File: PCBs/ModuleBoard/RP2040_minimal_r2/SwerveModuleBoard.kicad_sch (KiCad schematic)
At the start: 52 parts, among them J1 USB_B_Micro, J2 Conn_01x02, J4 Conn_01x07, J5 Conn_01x06_Pin, J6 Conn_01x02, J7 Conn_01x06_Pin, J8 Conn_01x06, U1 NCP1117-3.3_SOT223, U2 W25Q128JVS, U3 RP2040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

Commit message: vault backup: 2025-04-24 00:27:01
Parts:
- removed J2: Conn_01x02, Connector_PinHeader_2.54mm:PinHeader_1x02_P2.54mm_Vertical, symbol Connector_Generic:Conn_01x02
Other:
- moved on the sheet: BTSEL1
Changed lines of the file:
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@@
 	(wire
 		(pts
+			(xy 20.32 125.73) (xy 17.78 125.73)
+		)
+		(stroke
+			(width 0)
+			(type default)
+		)
+	)
+	(wire
+		(pts
 			(xy 39.37 204.47) (xy 46.99 204.47)
 		)
@@
 	(wire
 		(pts
-			(xy 44.45 125.73) (xy 31.75 125.73)
-		)
-		(stroke
-			(width 0)
-			(type default)
-		)
-	)
-	(wire
-		(pts
 			(xy 214.63 76.2) (xy 223.52 76.2)
 		)
@@
 	(wire
 		(pts
-			(xy 31.75 128.27) (xy 33.02 128.27)
-		)
-		(stroke
-			(width 0)
-			(type default)
-		)
-	)
-	(wire
-		(pts
 			(xy 234.95 60.96) (xy 246.38 60.96)
 		)
@@
 	(wire
 		(pts
+			(xy 30.48 125.73) (xy 44.45 125.73)
+		)
+		(stroke
+			(width 0)
+			(type default)
+		)
+	)
+	(wire
+		(pts
 			(xy 229.87 142.24) (xy 245.11 142.24)
 		)
@@
 	(wire
 		(pts
-			(xy 33.02 128.27) (xy 33.02 129.54)
-		)
-		(stroke
-			(width 0)
-			(type default)
-		)
-	)
-	(wire
-		(pts
 			(xy 97.79 105.41) (xy 97.79 120.65)
 		)
@@
 		)
 	)
-	(label "~{USB_BOOT}"
-		(at 36.83 109.22 0)
-		(effects
-			(font
-				(size 1.27 1.27)
-			)
-			(justify left bottom)
-		)
-	)
 	(label "GPIO14"
 		(at 245.11 147.32 180)
@@
 	)
 	(symbol
-		(lib_id "Connector_Generic:Conn_01x02")
-		(at 26.67 125.73 0)
-		(mirror y)
-		(unit 1)
-		(exclude_from_sim no)
-		(in_bom yes)
-		(on_board yes)
-		(dnp no)
-		(property "Reference" "J2"
-			(at 25.4 121.92 0)
-			(effects
-				(font
-					(size 1.27 1.27)
-				)
-			)
-		)
-		(property "Value" "Conn_01x02"
-			(at 25.4 132.08 0)
-			(effects
-				(font
-					(size 1.27 1.27)
-				)
-			)
-		)
-		(property "Footprint" "Connector_PinHeader_2.54mm:PinHeader_1x02_P2.54mm_Vertical"
-			(at 26.67 125.73 0)
-			(effects
-				(font
-					(size 1.27 1.27)
-				)
-				(hide yes)
-			)
-		)
-		(property "Datasheet" "~"
-			(at 26.67 125.73 0)
-			(effects
-				(font
-					(size 1.27 1.27)
-				)
-				(hide yes)
-			)
-		)
-		(property "Description" ""
-			(at 26.67 125.73 0)
-			(effects
-				(font
-					(size 1.27 1.27)
-				)
-				(hide yes)
-			)
-		)
-		(pin "1"
-		)
-		(pin "2"
-		)
-		(instances
-			(project "RP2040_minimal_r2"
-				(path "/8c0b3d8b-46d3-4173-ab1e-a61765f77d61"
-					(reference "J2")
-					(unit 1)
-				)
-			)
-		)
-	)
-	(symbol
-		(lib_id "power:GND")
-		(at 33.02 129.54 0)
-		(unit 1)
-		(exclude_from_sim no)
-		(in_bom yes)
-		(on_board yes)
-		(dnp no)
-		(property "Reference" "#PWR02"
-			(at 33.02 135.89 0)
-			(effects
-				(font
-					(size 1.27 1.27)
-				)
-				(hide yes)
-			)
-		)
-		(property "Value" "GND"
-			(at 33.147 133.9342 0)
-			(effects
-				(font
-					(size 1.27 1.27)
-				)
-			)
-		)
-		(property "Footprint" ""
-			(at 33.02 129.54 0)
-			(effects
-				(font
-					(size 1.27 1.27)
-				)
-				(hide yes)
-			)
-		)
-		(property "Datasheet" ""
-			(at 33.02 129.54 0)
-			(effects
-				(font
-					(size 1.27 1.27)
-				)
-				(hide yes)
-			)
-		)
-		(property "Description" ""
-			(at 33.02 129.54 0)
-			(effects
-				(font
-					(size 1.27 1.27)
-				)
-				(hide yes)
-			)
-		)
-		(pin "1"
-		)
-		(instances
-			(project "RP2040_minimal_r2"
-				(path "/8c0b3d8b-46d3-4173-ab1e-a61765f77d61"
-					(reference "#PWR02")
-					(unit 1)
-				)
-			)
-		)
-	)
-	(symbol
 		(lib_name "GND_4")
 		(lib_id "power:GND")
@@
 		(lib_name "GND_6")
 		(lib_id "power:GND")
-		(at 26.67 109.22 0)
+		(at 17.78 125.73 0)
 		(unit 1)
 		(exclude_from_sim no)
@@
 		(fields_autoplaced yes)
 		(property "Reference" "#PWR044"
-			(at 26.67 115.57 0)
+			(at 17.78 132.08 0)
 			(effects
 				(font
@@
 		)
 		(property "Value" "GND"
-			(at 26.67 114.3 0)
+			(at 17.78 130.81 0)
 			(effects
 				(font
@@
 		)
 		(property "Footprint" ""
-			(at 26.67 109.22 0)
+			(at 17.78 125.73 0)
 			(effects
 				(font
@@
 		)
 		(property "Datasheet" ""
-			(at 26.67 109.22 0)
+			(at 17.78 125.73 0)
 			(effects
 				(font
@@
 		)
 		(property "Description" "Power symbol creates a global label with name \"GND\" , ground"
-			(at 26.67 109.22 0)
+			(at 17.78 125.73 0)
 			(effects
 				(font
@@
 	(symbol
 		(lib_id "Switch:SW_Push")
-		(at 31.75 109.22 0)
+		(at 25.4 125.73 0)
 		(unit 1)
 		(exclude_from_sim no)
@@
 		(fields_autoplaced yes)
 		(property "Reference" "BTSEL1"
-			(at 31.75 101.6 0)
+			(at 25.4 118.11 0)
 			(effects
 				(font
@@
 		)
 		(property "Value" "SW_Push"
-			(at 31.75 104.14 0)
+			(at 25.4 120.65 0)
 			(effects
 				(font
@@
 		)
 		(property "Footprint" "Button_Switch_THT:SW_PUSH_6mm"
-			(at 31.75 104.14 0)
+			(at 25.4 120.65 0)
 			(effects
 				(font
@@
 		)
 		(property "Datasheet" "~"
-			(at 31.75 104.14 0)
+			(at 25.4 120.65 0)
 			(effects
 				(font
@@
 		)
 		(property "Description" "Push button switch, generic, two pins"
-			(at 31.75 109.22 0)
+			(at 25.4 125.73 0)
 			(effects
 				(font

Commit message: vault backup: 2025-04-24 01:46:54
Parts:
- added J2: Conn_02x08_Counter_Clockwise, Connector_PinHeader_2.54mm:PinHeader_2x08_P2.54mm_Vertical, symbol Connector_Generic:Conn_02x08_Counter_Clockwise
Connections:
- net GND: now also J2.11 (Pin_11), J2.12 (Pin_12), J2.13 (Pin_13), J2.4 (Pin_4), J2.5 (Pin_5), J2.6 (Pin_6)
- net GPIO4: now also J2.9 (Pin_9)
- net GPIO5: now also J2.8 (Pin_8)
- net VM: now also J2.1 (Pin_1), J2.14 (Pin_14), J2.15 (Pin_15), J2.16 (Pin_16), J2.2 (Pin_2), J2.3 (Pin_3)
- no-connect marks 1 -> 3
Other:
- moved on the sheet: J6

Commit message: vault backup: 2025-04-24 02:18:37
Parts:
- added C22: 100n, symbol Device:C
- added IC1: AS5600-ASOT, AS5600-ASOT:SOIC127P600X175-8N, symbol AS5600-ASOT:AS5600-ASOT
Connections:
- net +3V3: now also C22.1, IC1.1 (VDD5V), IC1.2 (VDD3V3), IC1.8 (DIR)
- net GND: now also C22.2, IC1.4 (GND)
- net GPIO4: now also IC1.6 (SDA)
- net GPIO5: now also IC1.7 (SCL)
- no-connect marks 3 -> 5
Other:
- note added: "AS5600"
- note added: "Main Connector"
- moved on the sheet: BTSEL1, C2, C3, C5, H1, H2, H3, H4, J2, J6, R1, R2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

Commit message: vault backup: 2025-04-24 02:23:43
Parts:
- removed J2: Conn_02x08_Counter_Clockwise, Connector_PinHeader_2.54mm:PinHeader_2x08_P2.54mm_Vertical, symbol Connector_Generic:Conn_02x08_Counter_Clockwise
- added J3: Conn_02x08_Odd_Even_MountingPin, symbol Connector_Generic_MountingPin:Conn_02x08_Odd_Even_MountingPin
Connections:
- net GND: now also J3.10 (Pin_10), J3.11 (Pin_11), J3.12 (Pin_12), J3.7 (Pin_7), J3.8 (Pin_8), J3.9 (Pin_9)
- net GPIO4: now also J3.16 (Pin_16)
- net GPIO5: now also J3.15 (Pin_15)
- net VM: now also J3.1 (Pin_1), J3.2 (Pin_2), J3.3 (Pin_3), J3.4 (Pin_4), J3.5 (Pin_5), J3.6 (Pin_6)
- no-connect marks 5 -> 6
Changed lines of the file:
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@@
 	)
 	(no_connect
+		(at 41.91 153.67)
+	)
+	(no_connect
 		(at 182.88 252.73)
 	)
@@
 	)
 	(symbol
-		(lib_id "Connector_Generic:Conn_02x08_Counter_Clockwise")
-		(at 40.64 138.43 0)
+		(lib_id "Device:LED")
+		(at 346.71 73.66 0)
 		(unit 1)
 		(exclude_from_sim no)
@@
 		(dnp no)
 		(fields_autoplaced yes)
-		(property "Reference" "J2"
-			(at 41.91 124.46 0)
+		(property "Reference" "D1"
+			(at 345.1225 67.31 0)
 			(effects
 				(font
@@
 			)
 		)
-		(property "Value" "Conn_02x08_Counter_Clockwise"
-			(at 41.91 127 0)
+		(property "Value" "LED"
+			(at 345.1225 69.85 0)
 			(effects
 				(font
@@
 			)
 		)
-		(property "Footprint" "Connector_PinHeader_2.54mm:PinHeader_2x08_P2.54mm_Vertical"
-			(at 40.64 138.43 0)
+		(property "Footprint" "LED_SMD:LED_0603_1608Metric_Pad1.05x0.95mm_HandSolder"
+			(at 346.71 73.66 0)
 			(effects
 				(font
@@
 		)
 		(property "Datasheet" "~"
-			(at 40.64 138.43 0)
+			(at 346.71 73.66 0)
 			(effects
 				(font
@@
 			)
 		)
-		(property "Description" "Generic connector, double row, 02x08, counter clockwise pin numbering scheme (similar to DIP package numbering), script generated (kicad-library-utils/schlib/autogen/connector/)"
-			(at 40.64 138.43 0)
+		(property "Description" "Light emitting diode"
+			(at 346.71 73.66 0)
 			(effects
 				(font
@@
 			)
 		)
-		(pin "10"
-		)
-		(pin "3"
-		)
-		(pin "7"
-		)
-		(pin "15"
-		)
-		(pin "11"
-		)
 		(pin "1"
 		)
-		(pin "4"
-		)
-		(pin "5"
-		)
-		(pin "6"
-		)
-		(pin "8"
-		)
-		(pin "14"
-		)
 		(pin "2"
 		)
-		(pin "13"
-		)
-		(pin "16"
-		)
-		(pin "12"
-		)
-		(pin "9"
-		)
 		(instances
 			(project ""
 				(path "/8c0b3d8b-46d3-4173-ab1e-a61765f77d61"
-					(reference "J2")
+					(reference "D1")
 					(unit 1)
 				)
@@
 	)
 	(symbol
-		(lib_id "Device:LED")
-		(at 346.71 73.66 0)
+		(lib_id "Connector_Generic_MountingPin:Conn_02x08_Odd_Even_MountingPin")
+		(at 40.64 138.43 0)
 		(unit 1)
 		(exclude_from_sim no)
@@
 		(dnp no)
 		(fields_autoplaced yes)
-		(property "Reference" "D1"
-			(at 345.1225 67.31 0)
+		(property "Reference" "J3"
+			(at 41.91 124.46 0)
 			(effects
 				(font
@@
 			)
 		)
-		(property "Value" "LED"
-			(at 345.1225 69.85 0)
+		(property "Value" "Conn_02x08_Odd_Even_MountingPin"
+			(at 41.91 127 0)
 			(effects
 				(font
@@
 			)
 		)
-		(property "Footprint" "LED_SMD:LED_0603_1608Metric_Pad1.05x0.95mm_HandSolder"
-			(at 346.71 73.66 0)
+		(property "Footprint" ""
+			(at 40.64 138.43 0)
 			(effects
 				(font
@@
 		)
 		(property "Datasheet" "~"
-			(at 346.71 73.66 0)
+			(at 40.64 138.43 0)
 			(effects
 				(font
@@
 			)
 		)
-		(property "Description" "Light emitting diode"
-			(at 346.71 73.66 0)
+		(property "Description" "Generic connectable mounting pin connector, double row, 02x08, odd/even pin numbering scheme (row 1 odd numbers, row 2 even numbers), script generated (kicad-library-utils/schlib/autogen/connector/)"
+			(at 40.64 138.43 0)
 			(effects
 				(font
@@
 			)
 		)
+		(pin "MP"
+		)
+		(pin "7"
+		)
+		(pin "4"
+		)
 		(pin "1"
 		)
+		(pin "5"
+		)
+		(pin "8"
+		)
+		(pin "3"
+		)
+		(pin "11"
+		)
+		(pin "15"
+		)
+		(pin "10"
+		)
 		(pin "2"
 		)
+		(pin "6"
+		)
+		(pin "14"
+		)
+		(pin "9"
+		)
+		(pin "13"
+		)
+		(pin "12"
+		)
+		(pin "16"
+		)
 		(instances
 			(project ""
 				(path "/8c0b3d8b-46d3-4173-ab1e-a61765f77d61"
-					(reference "D1")
+					(reference "J3")
 					(unit 1)
 				)

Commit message: vault backup: 2025-04-24 02:28:50
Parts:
- C22: footprint (none) -> Capacitor_SMD:C_0603_1608Metric
- J3: footprint (none) -> Connector_PinHeader_2.54mm:PinHeader_2x08_P2.54mm_Vertical
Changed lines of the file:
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@@
 			)
 		)
-		(property "Footprint" ""
+		(property "Footprint" "Capacitor_SMD:C_0603_1608Metric"
 			(at 178.7652 252.73 0)
 			(effects
@@
 			)
 		)
-		(property "Footprint" ""
+		(property "Footprint" "Connector_PinHeader_2.54mm:PinHeader_2x08_P2.54mm_Vertical"
 			(at 40.64 138.43 0)
 			(effects

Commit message: vault backup: 2025-04-24 02:39:03
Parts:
- IC1: footprint AS5600-ASOT:SOIC127P600X175-8N -> Package_SO:SOIC-8_3.9x4.9mm_P1.27mm
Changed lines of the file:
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@@
 			)
 		)
-		(property "Footprint" "AS5600-ASOT:SOIC127P600X175-8N"
+		(property "Footprint" "Package_SO:SOIC-8_3.9x4.9mm_P1.27mm"
 			(at 182.88 247.65 0)
 			(effects

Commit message: vault backup: 2025-04-24 02:44:10
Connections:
- net GPIO2: now also IC1.6 (SDA)
- net GPIO3: now also IC1.7 (SCL)
- net GPIO4: no longer IC1.6 (SDA)
- net GPIO5: no longer IC1.7 (SCL)
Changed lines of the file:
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@@
 		)
 	)
-	(label "SDA0"
+	(label "SDA1"
 		(at 213.36 252.73 0)
 		(effects
@@
 		)
 	)
+	(label "SDA1"
+		(at 247.65 116.84 0)
+		(effects
+			(font
+				(size 1.27 1.27)
+			)
+			(justify left bottom)
+		)
+	)
 	(label "GPIO0"
 		(at 245.11 111.76 180)
@@
 		)
 	)
+	(label "SCL1"
+		(at 247.65 119.38 0)
+		(effects
+			(font
+				(size 1.27 1.27)
+			)
+			(justify left bottom)
+		)
+	)
 	(label "QSPI_SCLK"
 		(at 152.4 128.27 0)
@@
 		)
 	)
-	(label "SCL0"
+	(label "SCL1"
 		(at 213.36 250.19 0)
 		(effects

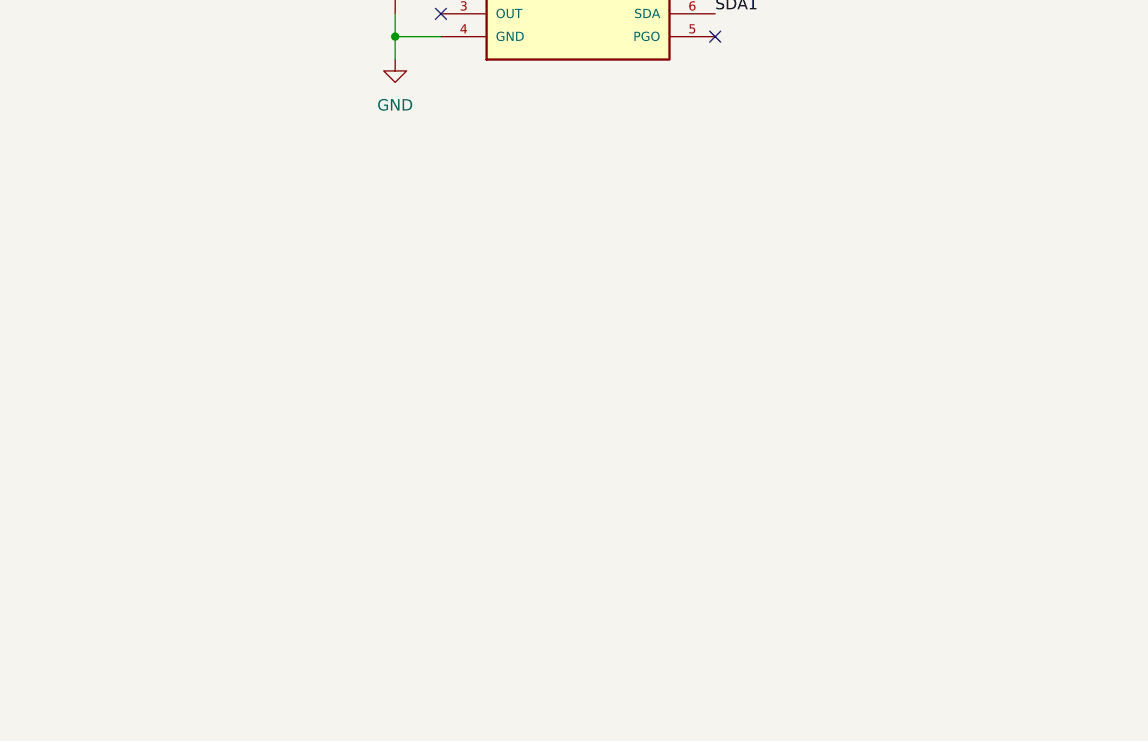
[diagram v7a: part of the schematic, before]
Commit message: added buck boost
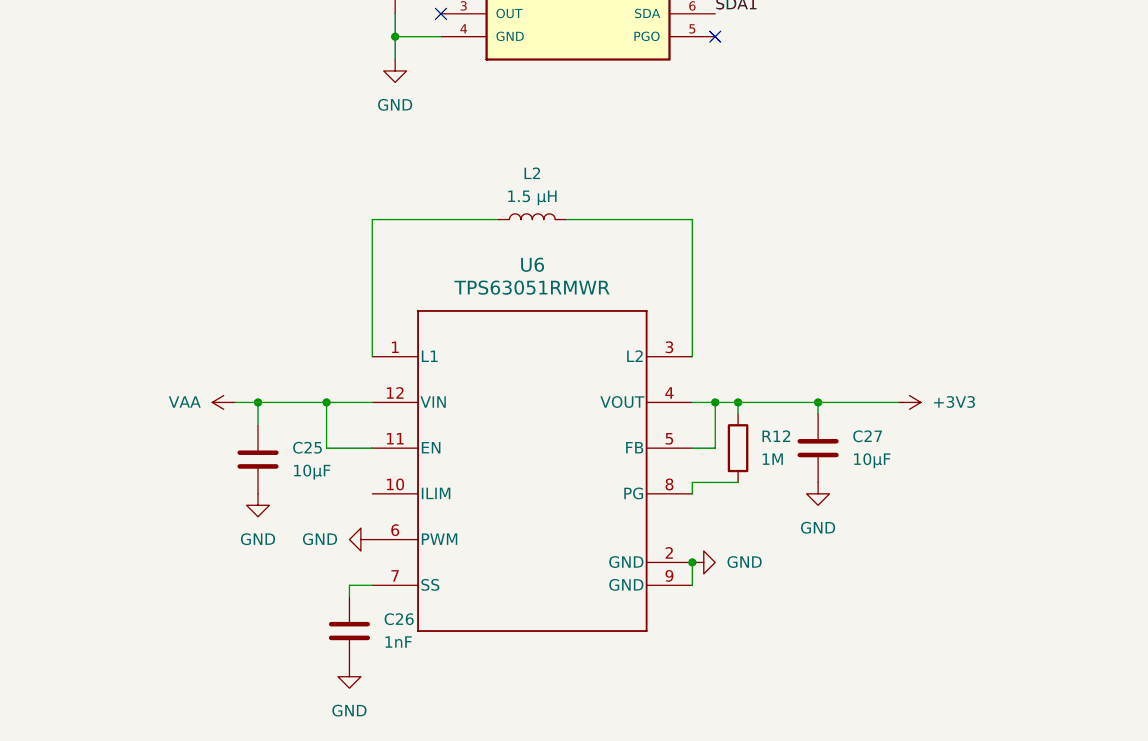
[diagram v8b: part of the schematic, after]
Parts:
- added C25, C27: 10μF, Capacitor_SMD:C_0603_1608Metric_Pad1.08x0.95mm_HandSolder, symbol Device:C
- added C26: 1nF, Capacitor_SMD:C_0603_1608Metric_Pad1.08x0.95mm_HandSolder, symbol Device:C
- added L2: 1.5 μH, Capacitor_SMD:C_0603_1608Metric_Pad1.08x0.95mm_HandSolder, symbol Device:L
- added R12: 1M, Resistor_SMD:R_0603_1608Metric_Pad0.98x0.95mm_HandSolder, symbol Device:R
- added U6: TPS63051RMWR, RMW0012A, symbol TPS63051:TPS63051RMWR
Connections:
- net +3V3: now also C27.1, R12.1, U6.4 (VOUT), U6.5 (FB)
- net GND: now also C25.2, C26.2, C27.2, U6.2 (GND), U6.6 (PWM), U6.9 (GND)
- new net: R12.2, U6.8 (PG)
- new net: L2.1, U6.1 (L1)
- new net: L2.2, U6.3 (L2)
- new net: C26.1, U6.7 (SS)
- new net VAA: C25.1, U6.11 (EN), U6.12 (VIN)
